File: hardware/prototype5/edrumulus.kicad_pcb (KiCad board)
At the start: 2 copper layers, 65 x 56.5 mm, 94 parts, among them J1 Trigger Connector, J2 Raspberry Pi GPIO pins, U1 ESP32-WROOM-32U, U2 AMS1117-3.3, U3 MCP1754S-3302xMB

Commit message: more routing prototype 5
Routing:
- net CRASH1-SLEEVE: track 326.0 -> 386.6 mm, vias 3 -> 4
- net SNARE-TIP: track 41.9 -> 45.0 mm, vias 0 -> 1
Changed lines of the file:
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@@
     (effects (font (size 1 1) (thickness 0.15)))
   )
+  (segment (start 163.83 102.182743) (end 163.83 96.52) (width 0.5) (layer "F.Cu") (net 1))
   (segment (start 145.296338 118.986194) (end 148.136338 121.826194) (width 0.25) (layer "F.Cu") (net 1))
   (segment (start 163.83 94.473691) (end 163.83 90.21937) (width 0.75) (layer "F.Cu") (net 1))
+  (segment (start 142.09 91.821) (end 146.805 96.536) (width 0.5) (layer "F.Cu") (net 1))
   (segment (start 150.14367 123.241492) (end 152.410507 123.241492) (width 0.25) (layer "F.Cu") (net 1))
   (segment (start 157.312104 88.908246) (end 161.108246 88.908246) (width 1) (layer "F.Cu") (net 1))
@@
   (segment (start 154.09046 96.94046) (end 153.67 96.52) (width 0.75) (layer "F.Cu") (net 1))
   (segment (start 127.953372 118.986194) (end 128.570306 118.986194) (width 0.25) (layer "F.Cu") (net 1))
-  (segment (start 150.217073 111.302946) (end 154.305 107.215019) (width 0.25) (layer "F.Cu") (net 1))
+  (segment (start 161.339361 103.475747) (end 161.339361 106.630639) (width 0.5) (layer "F.Cu") (net 1))
   (segment (start 130.18664 76.82336) (end 129.897713 77.112287) (width 0.25) (layer "F.Cu") (net 1))
   (segment (start 128.570306 118.986194) (end 131.410306 121.826194) (width 0.25) (layer "F.Cu") (net 1))
@@
   (segment (start 155.58664 75.846211) (end 155.58664 76.82336) (width 0.25) (layer "F.Cu") (net 1))
   (segment (start 157.140415 88.736557) (end 157.09143 88.785542) (width 1) (layer "F.Cu") (net 1))
-  (segment (start 161.339361 103.475747) (end 162.806846 102.008262) (width 0.25) (layer "F.Cu") (net 1))
+  (segment (start 154.305 111.302946) (end 154.305 106.036) (width 0.5) (layer "F.Cu") (net 1))
   (segment (start 150.206882 77.123118) (end 146.689733 77.123118) (width 0.25) (layer "F.Cu") (net 1))
   (segment (start 148.136338 121.826194) (end 148.728372 121.826194) (width 0.25) (layer "F.Cu") (net 1))
+  (segment (start 136.795 91.821) (end 138.045 91.821) (width 0.5) (layer "F.Cu") (net 1))
+  (segment (start 156.667054 111.302946) (end 149.319188 111.302946) (width 0.5) (layer "F.Cu") (net 1))
+  (segment (start 161.339361 103.475747) (end 162.536996 103.475747) (width 0.5) (layer "F.Cu") (net 1))
   (segment (start 125.10664 78.386211) (end 126.380564 77.112287) (width 0.25) (layer "F.Cu") (net 1))
   (segment (start 121.392129 77.2117) (end 123.932129 77.2117) (width 0.25) (layer "F.Cu") (net 1))
+  (segment (start 154.305 111.125) (end 152.883372 112.546628) (width 0.5) (layer "F.Cu") (net 1))
   (segment (start 140.418372 121.826194) (end 140.418372 120.291016) (width 0.25) (layer "F.Cu") (net 1))
   (segment (start 133.500549 123.218371) (end 132.108372 121.826194) (width 0.25) (layer "F.Cu") (net 1))
   (segment (start 157.140415 88.736557) (end 157.312104 88.908246) (width 1) (layer "F.Cu") (net 1))
   (segment (start 144.573372 118.986194) (end 145.296338 118.986194) (width 0.25) (layer "F.Cu") (net 1))
+  (segment (start 154.305 106.036) (end 154.305 111.125) (width 0.5) (layer "F.Cu") (net 1))
   (segment (start 120.02664 75.846211) (end 121.392129 77.2117) (width 0.25) (layer "F.Cu") (net 1))
   (segment (start 162.806846 95.496846) (end 163.83 94.473691) (width 0.75) (layer "F.Cu") (net 1))
@@
   (segment (start 127 95.25) (end 127 96.52) (width 0.5) (layer "F.Cu") (net 1))
   (segment (start 140.418372 121.826194) (end 139.026195 123.218371) (width 0.25) (layer "F.Cu") (net 1))
+  (segment (start 152.883372 112.546628) (end 152.883372 118.986194) (width 0.5) (layer "F.Cu") (net 1))
   (segment (start 155.58664 76.82336) (end 155.286882 77.123118) (width 0.25) (layer "F.Cu") (net 1))
+  (segment (start 138.045 91.821) (end 139.7 93.476) (width 0.5) (layer "F.Cu") (net 1))
+  (segment (start 149.319188 111.302946) (end 154.305 111.302946) (width 0.5) (layer "F.Cu") (net 1))
+  (segment (start 136.795 91.821) (end 142.09 91.821) (width 0.5) (layer "F.Cu") (net 1))
   (segment (start 137.80664 75.846211) (end 137.80664 76.82336) (width 0.25) (layer "F.Cu") (net 1))
+  (segment (start 163.83 96.52) (end 162.806846 95.496846) (width 0.5) (layer "F.Cu") (net 1))
   (segment (start 155.286882 77.123118) (end 150.206882 77.123118) (width 0.25) (layer "F.Cu") (net 1))
-  (segment (start 154.305 107.215019) (end 154.305 106.036) (width 0.25) (layer "F.Cu") (net 1))
   (segment (start 162.75063 89.14) (end 161.34 89.14) (width 0.75) (layer "F.Cu") (net 1))
   (segment (start 146.689733 77.123118) (end 145.42664 78.386211) (width 0.25) (layer "F.Cu") (net 1))
@@
   (segment (start 141.723194 118.986194) (end 141.803372 118.986194) (width 0.25) (layer "F.Cu") (net 1))
   (segment (start 123.932129 77.2117) (end 125.10664 78.386211) (width 0.25) (layer "F.Cu") (net 1))
+  (segment (start 161.339361 106.630639) (end 156.667054 111.302946) (width 0.5) (layer "F.Cu") (net 1))
+  (segment (start 139.7 93.476) (end 139.7 100.33) (width 0.5) (layer "F.Cu") (net 1))
   (segment (start 163.20664 78.386211) (end 161.943547 77.123118) (width 0.25) (layer "F.Cu") (net 1))
   (segment (start 150.50664 76.82336) (end 150.206882 77.123118) (width 0.25) (layer "F.Cu") (net 1))
   (segment (start 161.108246 88.908246) (end 161.34 89.14) (width 1) (layer "F.Cu") (net 1))
-  (segment (start 149.319188 111.302946) (end 150.217073 111.302946) (width 0.25) (layer "F.Cu") (net 1))
   (segment (start 150.50664 75.846211) (end 150.50664 76.82336) (width 0.25) (layer "F.Cu") (net 1))
   (segment (start 130.18664 75.846211) (end 130.18664 76.82336) (width 0.25) (layer "F.Cu") (net 1))
@@
   (segment (start 157.181549 96.94046) (end 154.09046 96.94046) (width 0.75) (layer "F.Cu") (net 1))
   (segment (start 152.883372 122.768627) (end 152.883372 118.986194) (width 0.25) (layer "F.Cu") (net 1))
-  (segment (start 162.806846 102.008262) (end 162.806846 95.496846) (width 0.25) (layer "F.Cu") (net 1))
+  (segment (start 162.536996 103.475747) (end 163.83 102.182743) (width 0.5) (layer "F.Cu") (net 1))
   (segment (start 126.380564 77.112287) (end 129.897713 77.112287) (width 0.25) (layer "F.Cu") (net 1))
   (via (at 129.132044 93.117956) (size 0.8) (drill 0.4) (layers "F.Cu" "B.Cu") (net 1))
   (via (at 127 96.52) (size 0.8) (drill 0.4) (layers "F.Cu" "B.Cu") (net 1))
+  (via (at 139.7 100.33) (size 0.8) (drill 0.4) (layers "F.Cu" "B.Cu") (net 1))
   (via (at 153.67 96.52) (size 0.8) (drill 0.4) (layers "F.Cu" "B.Cu") (net 1))
   (segment (start 139.42274 103.868814) (end 141.283814 103.868814) (width 0.5) (layer "B.Cu") (net 1))
@@
   (segment (start 150.011628 93.119333) (end 150.384962 92.745999) (width 0.5) (layer "B.Cu") (net 1))
   (segment (start 160.647572 93.246775) (end 160.987088 92.907259) (width 0.5) (layer "B.Cu") (net 1))
+  (segment (start 139.7 100.33) (end 139.42274 100.60726) (width 0.5) (layer "B.Cu") (net 1))
   (segment (start 114.641485 73.964938) (end 113.566239 75.040184) (width 0.5) (layer "B.Cu") (net 1))
   (segment (start 124.317288 93.038977) (end 126.638102 93.038977) (width 0.5) (layer "B.Cu") (net 1))
@@
   (segment (start 114.3 96.382516) (end 114.3 100.33) (width 0.5) (layer "B.Cu") (net 1))
   (segment (start 128.305367 73.964938) (end 114.641485 73.964938) (width 0.5) (layer "B.Cu") (net 1))
+  (segment (start 139.42274 100.60726) (end 139.42274 103.868814) (width 0.5) (layer "B.Cu") (net 1))
   (segment (start 114.3 100.33) (end 113.18277 100.33) (width 0.5) (layer "B.Cu") (net 1))
   (segment (start 130.18664 75.846211) (end 128.305367 73.964938) (width 0.5) (layer "B.Cu") (net 1))
@@
   (segment (start 166.003966 113.396034) (end 152.933532 113.396034) (width 0.25) (layer "B.Cu") (net 29))
   (segment (start 170.18 109.22) (end 166.003966 113.396034) (width 0.25) (layer "B.Cu") (net 29))
+  (segment (start 165.1 109.22) (end 158.75 115.57) (width 0.25) (layer "F.Cu") (net 30))
   (segment (start 167.874785 84.402859) (end 167.874785 86.125215) (width 0.25) (layer "F.Cu") (net 30))
-  (segment (start 165.1 88.9) (end 165.1 103.999566) (width 0.25) (layer "F.Cu") (net 30))
   (segment (start 167.874785 86.125215) (end 165.1 88.9) (width 0.25) (layer "F.Cu") (net 30))
-  (segment (start 165.1 103.999566) (end 150.113372 118.986194) (width 0.25) (layer "F.Cu") (net 30))
+  (segment (start 165.1 88.9) (end 165.1 109.22) (width 0.25) (layer "F.Cu") (net 30))
+  (via (at 158.75 115.57) (size 0.8) (drill 0.4) (layers "F.Cu" "B.Cu") (net 30))
+  (segment (start 158.75 115.57) (end 153.529566 115.57) (width 0.25) (layer "B.Cu") (net 30))
+  (segment (start 153.529566 115.57) (end 150.113372 118.986194) (width 0.25) (layer "B.Cu") (net 30))
   (segment (start 169.710132 81.405261) (end 170.517436 82.212564) (width 0.25) (layer "F.Cu") (net 31))
   (segment (start 157.038045 118.986194) (end 155.653372 118.986194) (width 0.25) (layer "F.Cu") (net 31))

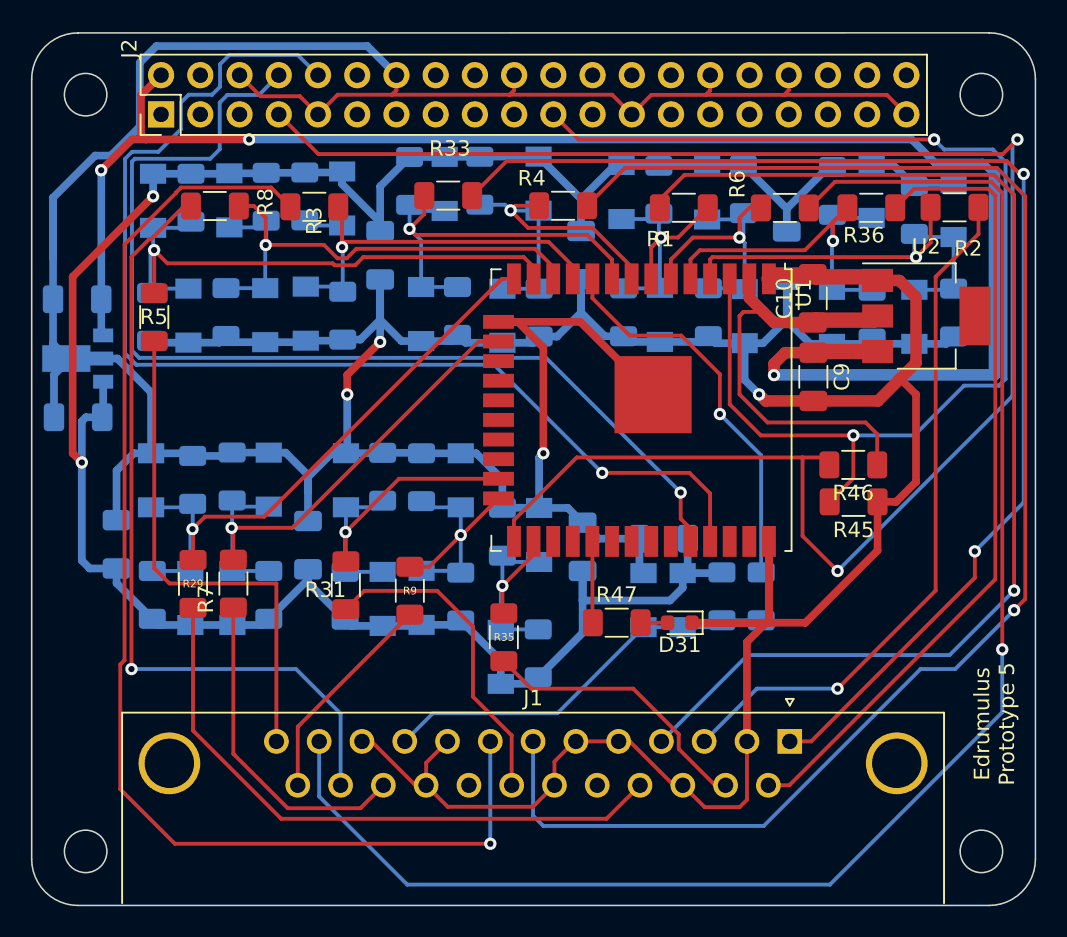
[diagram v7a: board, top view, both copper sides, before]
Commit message: use additional GND line for ESP32
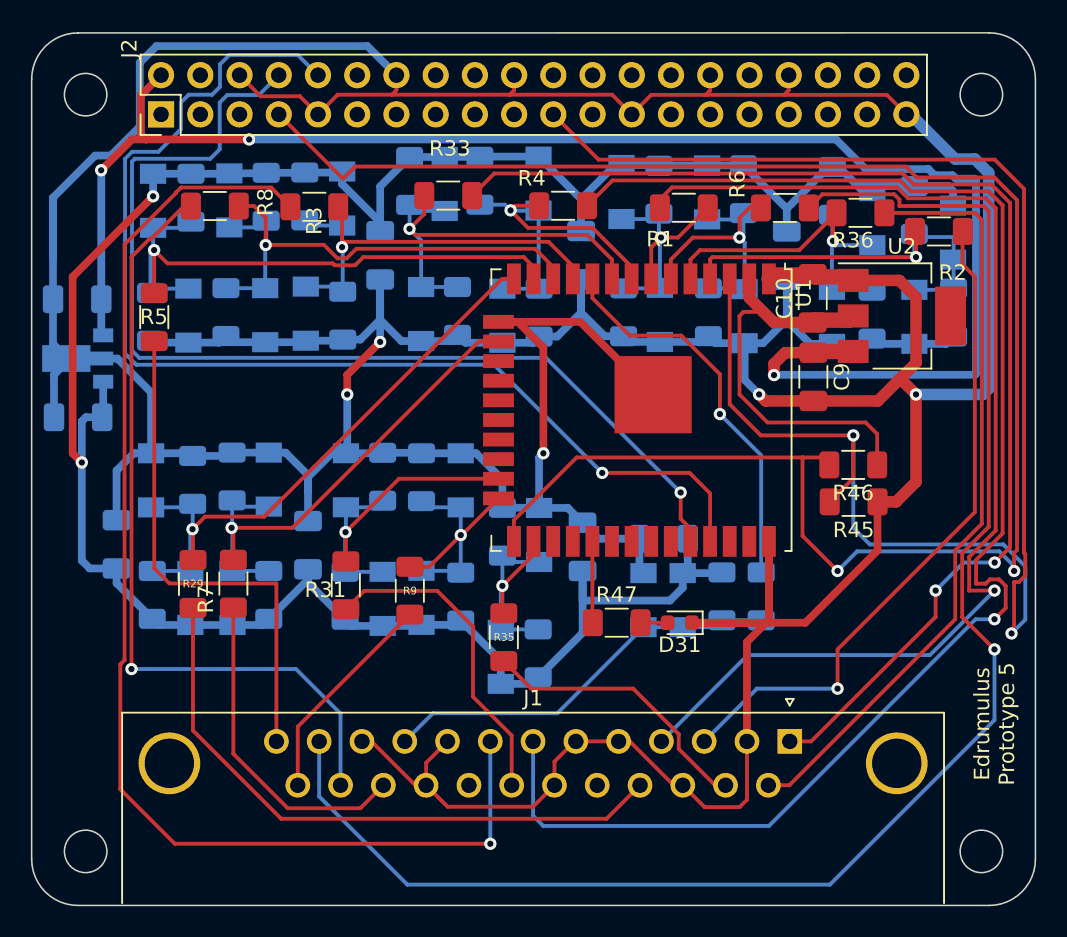
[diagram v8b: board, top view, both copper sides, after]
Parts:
- moved R2 1.86 mm to (165.3, 86.0)
- moved D30 1.76 mm to (161.0, 85.1)
- moved U2 1.58 mm to (162.9, 91.4)
- moved D11 1.46 mm to (166.2, 86.0)
- moved R36 0.77 mm to (160.2, 84.8)
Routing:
- net PI-GPIO9: track 77.9 -> 106.6 mm
- net CRASH1-SLEEVE: track 386.6 -> 412.4 mm, vias 4 -> 5
- net PI-GPIO4: track 114.0 -> 119.5 mm
- net RASPI-VIN: track 110.2 -> 106.0 mm
- net TOM1-TIP: track 52.2 -> 49.6 mm
- net KICK-TIP: track 81.0 -> 79.0 mm
- net GPIO36: track 28.4 -> 26.5 mm
- net ESP32-3V3: track 29.1 -> 27.5 mm
- net SNARE-TIP: track 45.0 -> 43.7 mm
- net SNARE-RING: track 77.2 -> 75.9 mm
- net 3V3: track 161.4 -> 162.6 mm
- net HI-HAT-TIP: track 99.3 -> 98.6 mm
- net CRASH1-TIP: track 101.9 -> 101.3 mm
